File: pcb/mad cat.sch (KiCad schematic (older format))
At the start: 262 parts, among them J1 Conn_01x04, J2 Conn_02x03_Odd_Even, SW0,0 ESC, SW0,1 ESC/F1, SW0,10 F9, SW0,10-1 F10, SW0,11 F10, SW0,11-1 F11, SW0,12 F11, SW0,12-1 F12, SW0,13 F12/PRT, SW0,14 INS, SW0,15 HOME, SW0,16 PGUP, SW0,2 F1, SW0,2-1 F2, SW0,3 F2, SW0,3-1 F3, SW0,4 F3, SW0,4-1 F4, SW0,5 F4, SW0,5-1 F5, SW0,6 F5, SW0,6-1 F6, SW0,7 F6, SW0,7-1 F7, SW0,8 F7, SW0,8-1 F8, SW0,9 F8, SW0,9-1 F9, SW1,0 PF1, SW1,0-1 PF1, SW1,1 TILDE, SW1,10 9, SW1,11 0, SW1,12 -, SW1,13 =, SW1,14 BACKSPACE, SW1,14-1 S_BS_L, SW1,15 END, SW1,16 PGDN, SW1,2 1, SW1,3 2, SW1,4 3, SW1,5 4, SW1,6 5, SW1,7 6, SW1,8 7, SW1,9 8, SW2,0 PF2, SW2,0-1 PF2, SW2,1 TAB, SW2,10 O, SW2,11 P, SW2,12 [, SW2,13 ], SW2,14 \\, SW2,15 S_BS_R, SW2,16 PRT, SW2,2 Q, SW2,3 W, SW2,4 E, SW2,5 R, SW2,6 T, SW2,7 Y, SW2,8 U, SW2,9 I, SW3,0 PF3, SW3,0-1 PF3, SW3,1 CAPS, SW3,1-1 ST_CAPS, SW3,10 L, SW3,11 COLONS, SW3,12 QUOTE, SW3,13 ISO_#, SW3,14 ENT, SW3,14-1 ISO_ENT, SW3,15 DEL, SW3,15-1 DEL, SW3,15-2 DEL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

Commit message: little updates
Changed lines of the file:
@@
 Wire Wire Line
 	400  2750 750  2750
-Connection ~ 750  2750
-Wire Wire Line
-	750  2750 1500 2750
-Connection ~ 1500 2750
 Connection ~ 2250 2750
 Wire Wire Line
@@
 $EndComp
 Connection ~ 1350 3950
-Wire Wire Line
-	1350 3950 1350 3550
 Wire Wire Line
 	750  3950 750  4050
@@
 Wire Wire Line
 	1350 1100 1350 1250
-Wire Wire Line
-	750  1550 750  1250
 Connection ~ 750  1550
 Wire Wire Line
 	950  1250 1350 1250
-Wire Wire Line
-	1350 1250 1350 1550
 Connection ~ 1350 1250
 Wire Wire Line
@@
 Connection ~ 1350 3450
 Wire Wire Line
-	1350 3450 1350 3050
-Wire Wire Line
 	750  3450 750  3550
 Connection ~ 750  3550
@@
 Connection ~ 1350 2950
 Wire Wire Line
-	1350 2950 1350 2550
-Wire Wire Line
 	750  2950 750  3050
 Connection ~ 750  3050
@@
 Connection ~ 1350 2450
 Wire Wire Line
-	1350 2450 1350 2050
-Wire Wire Line
 	750  2450 750  2550
 Connection ~ 750  2550
@@
 Connection ~ 1350 1950
 Wire Wire Line
-	1350 1950 1350 1550
-Wire Wire Line
 	750  1950 750  2050
 Connection ~ 750  2050
@@
 	12000 3450 12000 3550
 Connection ~ 12000 3550
+Wire Wire Line
+	1350 1550 1350 1950
+Wire Wire Line
+	750  1250 750  1550
+Wire Wire Line
+	1350 1250 1350 1550
+Wire Wire Line
+	1350 3550 1350 3950
+Wire Wire Line
+	1350 3050 1350 3450
+Connection ~ 1500 2750
+Connection ~ 750  2750
+Wire Wire Line
+	750  2750 1500 2750
+Wire Wire Line
+	1350 2550 1350 2950
+Wire Wire Line
+	1350 2050 1350 2450
 $EndSCHEMATC

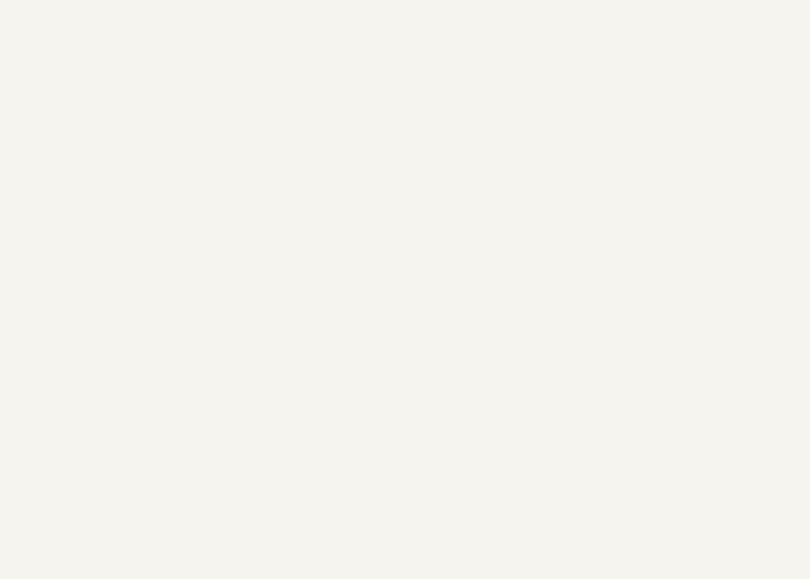
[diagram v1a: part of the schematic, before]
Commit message: changed holes to m2.5
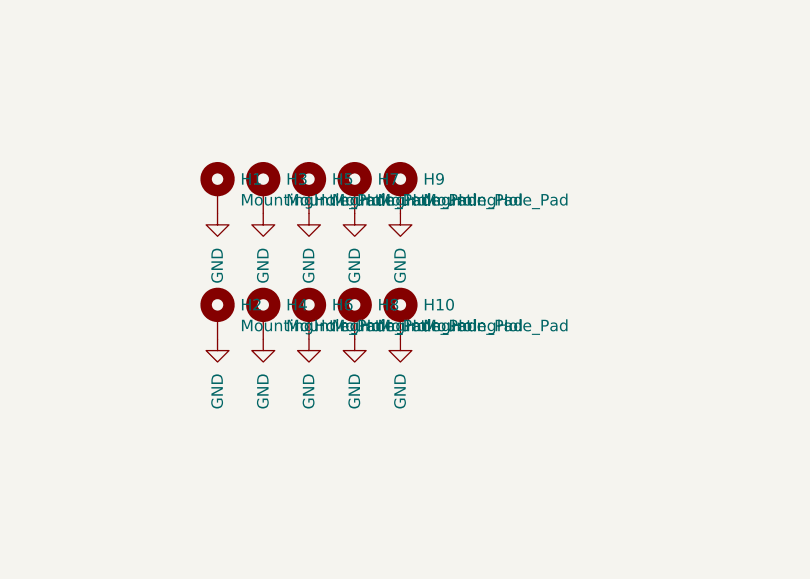
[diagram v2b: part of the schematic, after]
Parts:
- added H1, H10, H2, H3, H4, H5, H6, H7, H8, H9: MountingHole_Pad, keebs:m2.5_pad_via, symbol Mechanical:MountingHole_Pad
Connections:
- net GND: now also H1.1, H10.1, H2.1, H3.1, H4.1, H5.1, H6.1, H7.1, H8.1, H9.1
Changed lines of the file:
@@
 Wire Wire Line
 	1350 2050 1350 2450
+$Comp
+L Mechanical:MountingHole_Pad H1
+U 1 1 5CEC3121
+P 1300 5750
+F 0 "H1" H 1400 5799 50  0000 L CNN
+F 1 "MountingHole_Pad" H 1400 5708 50  0000 L CNN
+F 2 "keebs:m2.5_pad_via" H 1300 5750 50  0001 C CNN
+F 3 "~" H 1300 5750 50  0001 C CNN
+	1    1300 5750
+	1    0    0    -1
+$EndComp
+$Comp
+L power:GND #PWR011
+U 1 1 5CEC4BEC
+P 1300 5850
+F 0 "#PWR011" H 1300 5600 50  0001 C CNN
+F 1 "GND" V 1300 5700 50  0000 R CNN
+F 2 "" H 1300 5850 50  0001 C CNN
+F 3 "" H 1300 5850 50  0001 C CNN
+	1    1300 5850
+	1    0    0    -1
+$EndComp
+$Comp
+L Mechanical:MountingHole_Pad H3
+U 1 1 5CEC7481
+P 1500 5750
+F 0 "H3" H 1600 5799 50  0000 L CNN
+F 1 "MountingHole_Pad" H 1600 5708 50  0000 L CNN
+F 2 "keebs:m2.5_pad_via" H 1500 5750 50  0001 C CNN
+F 3 "~" H 1500 5750 50  0001 C CNN
+	1    1500 5750
+	1    0    0    -1
+$EndComp
+$Comp
+L power:GND #PWR030
+U 1 1 5CEC7487
+P 1500 5850
+F 0 "#PWR030" H 1500 5600 50  0001 C CNN
+F 1 "GND" V 1500 5700 50  0000 R CNN
+F 2 "" H 1500 5850 50  0001 C CNN
+F 3 "" H 1500 5850 50  0001 C CNN
+	1    1500 5850
+	1    0    0    -1
+$EndComp
+$Comp
+L Mechanical:MountingHole_Pad H5
+U 1 1 5CEE69D2
+P 1700 5750
+F 0 "H5" H 1800 5799 50  0000 L CNN
+F 1 "MountingHole_Pad" H 1800 5708 50  0000 L CNN
+F 2 "keebs:m2.5_pad_via" H 1700 5750 50  0001 C CNN
+F 3 "~" H 1700 5750 50  0001 C CNN
+	1    1700 5750
+	1    0    0    -1
+$EndComp
+$Comp
+L power:GND #PWR032
+U 1 1 5CEE69D8
+P 1700 5850
+F 0 "#PWR032" H 1700 5600 50  0001 C CNN
+F 1 "GND" V 1700 5700 50  0000 R CNN
+F 2 "" H 1700 5850 50  0001 C CNN
+F 3 "" H 1700 5850 50  0001 C CNN
+	1    1700 5850
+	1    0    0    -1
+$EndComp
+$Comp
+L Mechanical:MountingHole_Pad H7
+U 1 1 5CF05E57
+P 1900 5750
+F 0 "H7" H 2000 5799 50  0000 L CNN
+F 1 "MountingHole_Pad" H 2000 5708 50  0000 L CNN
+F 2 "keebs:m2.5_pad_via" H 1900 5750 50  0001 C CNN
+F 3 "~" H 1900 5750 50  0001 C CNN
+	1    1900 5750
+	1    0    0    -1
+$EndComp
+$Comp
+L power:GND #PWR034
+U 1 1 5CF05E5D
+P 1900 5850
+F 0 "#PWR034" H 1900 5600 50  0001 C CNN
+F 1 "GND" V 1900 5700 50  0000 R CNN
+F 2 "" H 1900 5850 50  0001 C CNN
+F 3 "" H 1900 5850 50  0001 C CNN
+	1    1900 5850
+	1    0    0    -1
+$EndComp
+$Comp
+L Mechanical:MountingHole_Pad H2
+U 1 1 5CF254C4
+P 1300 6300
+F 0 "H2" H 1400 6349 50  0000 L CNN
+F 1 "MountingHole_Pad" H 1400 6258 50  0000 L CNN
+F 2 "keebs:m2.5_pad_via" H 1300 6300 50  0001 C CNN
+F 3 "~" H 1300 6300 50  0001 C CNN
+	1    1300 6300
+	1    0    0    -1
+$EndComp
+$Comp
+L power:GND #PWR016
+U 1 1 5CF254CA
+P 1300 6400
+F 0 "#PWR016" H 1300 6150 50  0001 C CNN
+F 1 "GND" V 1300 6250 50  0000 R CNN
+F 2 "" H 1300 6400 50  0001 C CNN
+F 3 "" H 1300 6400 50  0001 C CNN
+	1    1300 6400
+	1    0    0    -1
+$EndComp
+$Comp
+L Mechanical:MountingHole_Pad H4
+U 1 1 5CF44A2D
+P 1500 6300
+F 0 "H4" H 1600 6349 50  0000 L CNN
+F 1 "MountingHole_Pad" H 1600 6258 50  0000 L CNN
+F 2 "keebs:m2.5_pad_via" H 1500 6300 50  0001 C CNN
+F 3 "~" H 1500 6300 50  0001 C CNN
+	1    1500 6300
+	1    0    0    -1
+$EndComp
+$Comp
+L power:GND #PWR031
+U 1 1 5CF44A33
+P 1500 6400
+F 0 "#PWR031" H 1500 6150 50  0001 C CNN
+F 1 "GND" V 1500 6250 50  0000 R CNN
+F 2 "" H 1500 6400 50  0001 C CNN
+F 3 "" H 1500 6400 50  0001 C CNN
+	1    1500 6400
+	1    0    0    -1
+$EndComp
+$Comp
+L Mechanical:MountingHole_Pad H6
+U 1 1 5CF64138
+P 1700 6300
+F 0 "H6" H 1800 6349 50  0000 L CNN
+F 1 "MountingHole_Pad" H 1800 6258 50  0000 L CNN
+F 2 "keebs:m2.5_pad_via" H 1700 6300 50  0001 C CNN
+F 3 "~" H 1700 6300 50  0001 C CNN
+	1    1700 6300
+	1    0    0    -1
+$EndComp
+$Comp
+L power:GND #PWR033
+U 1 1 5CF6413E
+P 1700 6400
+F 0 "#PWR033" H 1700 6150 50  0001 C CNN
+F 1 "GND" V 1700 6250 50  0000 R CNN
+F 2 "" H 1700 6400 50  0001 C CNN
+F 3 "" H 1700 6400 50  0001 C CNN
+	1    1700 6400
+	1    0    0    -1
+$EndComp
+$Comp
+L Mechanical:MountingHole_Pad H8
+U 1 1 5CF836A1
+P 1900 6300
+F 0 "H8" H 2000 6349 50  0000 L CNN
+F 1 "MountingHole_Pad" H 2000 6258 50  0000 L CNN
+F 2 "keebs:m2.5_pad_via" H 1900 6300 50  0001 C CNN
+F 3 "~" H 1900 6300 50  0001 C CNN
+	1    1900 6300
+	1    0    0    -1
+$EndComp
+$Comp
+L power:GND #PWR035
+U 1 1 5CF836A7
+P 1900 6400
+F 0 "#PWR035" H 1900 6150 50  0001 C CNN
+F 1 "GND" V 1900 6250 50  0000 R CNN
+F 2 "" H 1900 6400 50  0001 C CNN
+F 3 "" H 1900 6400 50  0001 C CNN
+	1    1900 6400
+	1    0    0    -1
+$EndComp
+$Comp
+L Mechanical:MountingHole_Pad H9
+U 1 1 5CFC6FD9
+P 2100 5750
+F 0 "H9" H 2200 5799 50  0000 L CNN
+F 1 "MountingHole_Pad" H 2200 5708 50  0000 L CNN
+F 2 "keebs:m2.5_pad_via" H 2100 5750 50  0001 C CNN
+F 3 "~" H 2100 5750 50  0001 C CNN
+	1    2100 5750
+	1    0    0    -1
+$EndComp
+$Comp
+L power:GND #PWR036
+U 1 1 5CFC6FDF
+P 2100 5850
+F 0 "#PWR036" H 2100 5600 50  0001 C CNN
+F 1 "GND" V 2100 5700 50  0000 R CNN
+F 2 "" H 2100 5850 50  0001 C CNN
+F 3 "" H 2100 5850 50  0001 C CNN
+	1    2100 5850
+	1    0    0    -1
+$EndComp
+$Comp
+L Mechanical:MountingHole_Pad H10
+U 1 1 5CFE6828
+P 2100 6300
+F 0 "H10" H 2200 6349 50  0000 L CNN
+F 1 "MountingHole_Pad" H 2200 6258 50  0000 L CNN
+F 2 "keebs:m2.5_pad_via" H 2100 6300 50  0001 C CNN
+F 3 "~" H 2100 6300 50  0001 C CNN
+	1    2100 6300
+	1    0    0    -1
+$EndComp
+$Comp
+L power:GND #PWR037
+U 1 1 5CFE682E
+P 2100 6400
+F 0 "#PWR037" H 2100 6150 50  0001 C CNN
+F 1 "GND" V 2100 6250 50  0000 R CNN
+F 2 "" H 2100 6400 50  0001 C CNN
+F 3 "" H 2100 6400 50  0001 C CNN
+	1    2100 6400
+	1    0    0    -1
+$EndComp
 $EndSCHEMATC

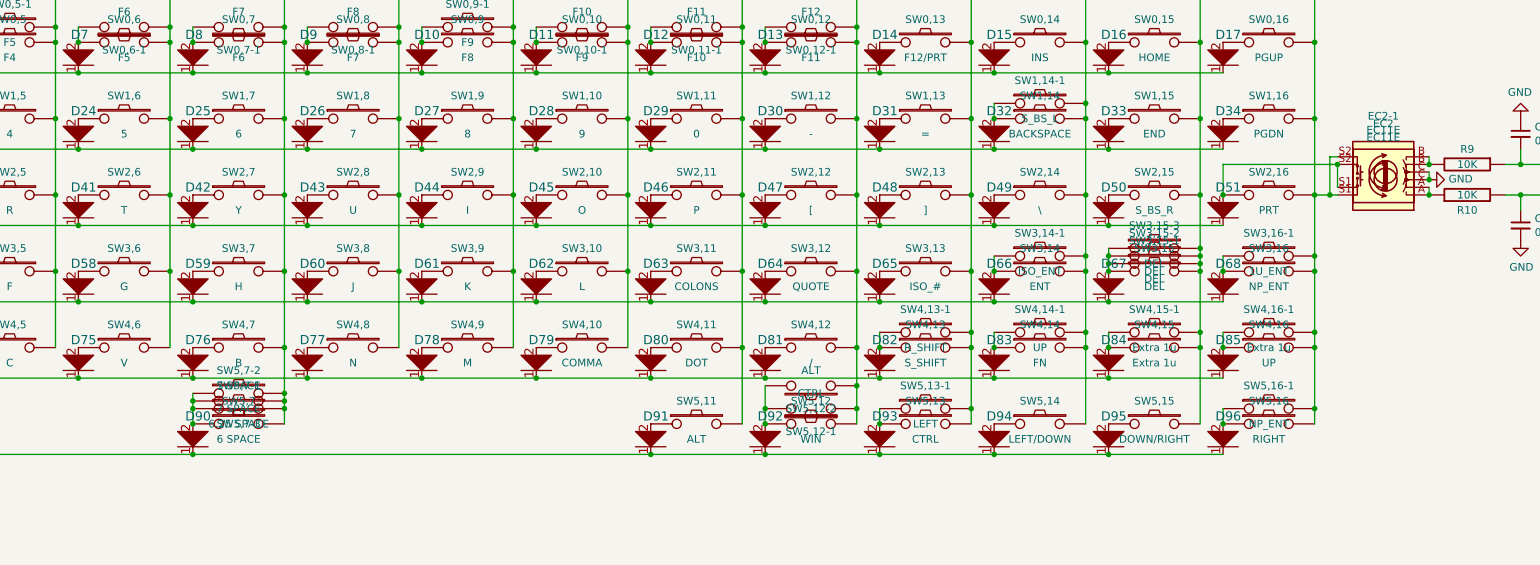
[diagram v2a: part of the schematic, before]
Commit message: redo layout after ic
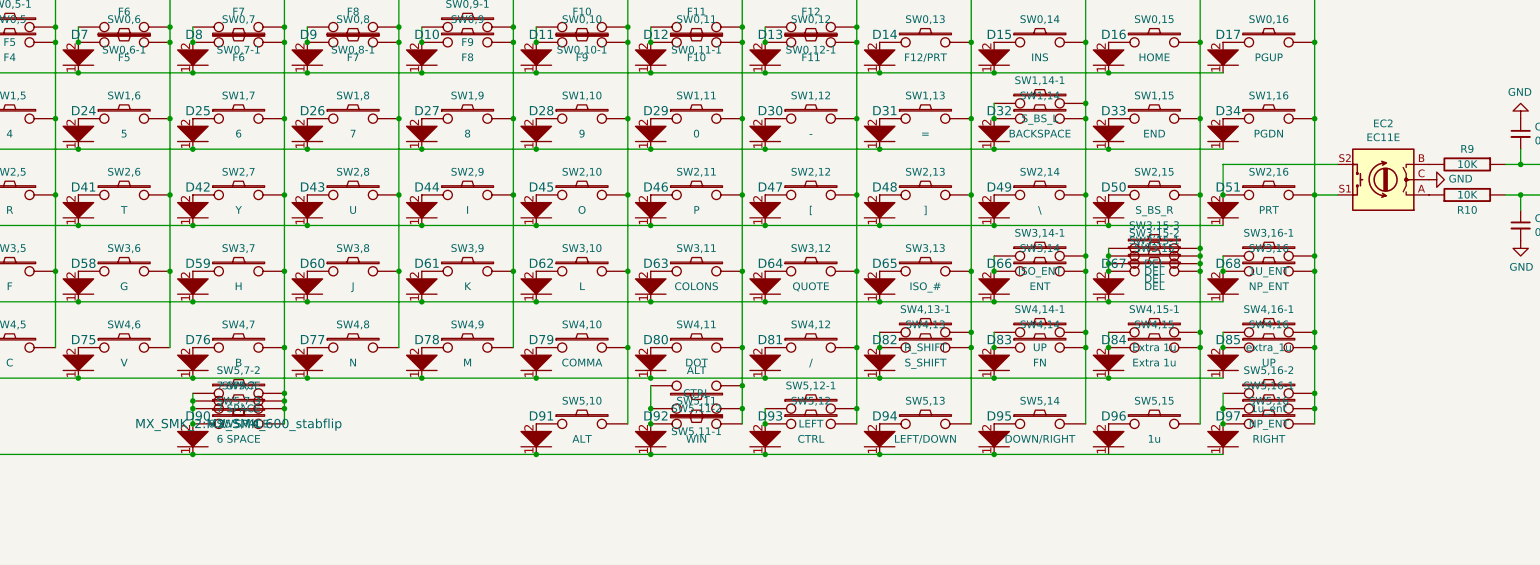
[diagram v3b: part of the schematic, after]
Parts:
- removed EC2-1: EC11E, keebs:EC11E, symbol Device:Rotary_Encoder_Switch
- removed SW5,7: 6 SPACE, MX_SMK_2:MX_600_stabflip, symbol keyboard_parts:SW_PUSH
- added D96: D, Diode_SMD:D_SOD-123, symbol keyboard_parts:D
- added SW5,15: 1u, MX_SMK_2:MX_100, symbol keyboard_parts:SW_PUSH
- added SW5,16-2: 1u_ent, MX_SMK_2:MX_100, symbol keyboard_parts:SW_PUSH
- added SW5,7-3: 6 SPACE, MX_SMK_2:MX_SMK_600_stabflip, symbol keyboard_parts:SW_PUSH
- SW3,15, SW3,15-1: footprint MX_SMK_2:MX_200 -> MX_SMK_2:MX_200_stabflip
- SW4,16-1: value Extra 1u -> extra_1u
- renumbered D96 to D97, SW5,11 to SW5,10, SW5,12 to SW5,11, SW5,12-1 to SW5,11-1, SW5,12-2 to SW5,11-2, SW5,13 to SW5,12, SW5,13-1 to SW5,12-1, SW5,14 to SW5,13, SW5,15 to SW5,14, SW5,7-1 to SW5,7, SW5,7-3 to SW5,7-1
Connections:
- net c10: now also SW5,10.2
- net c11: now also SW5,11-1.1, SW5,11-2.1, SW5,11.2; no longer SW5,10.2
- net c12: now also SW5,12-1.2, SW5,12.2; no longer SW5,11-1.1, SW5,11-2.1, SW5,11.2
- net c13: now also SW5,13.2; no longer SW5,12-1.2, SW5,12.2
- net c14: now also SW5,14.2; no longer SW5,13.2
- net c15: now also SW5,15.2; no longer SW5,14.2
- net c16: now also SW5,16-2.2
- net c7: now also SW5,7-3.2
- net at D90.2, SW5,7-1.2, SW5,7-2.1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: now also SW5,7-3.1
- net at D97.2, SW5,16-1.1, SW5,16.1: now also SW5,16-2.1
- new net: D96.2, SW5,15.1
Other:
- moved on the sheet: D91, D92, D93, D94, D95, SW5,10, SW5,11, SW5,11-1, SW5,11-2, SW5,12, SW5,12-1, SW5,13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

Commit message: progress on redo
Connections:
- net r5: now also D96.1
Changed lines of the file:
@@
 Connection ~ 11250 4250
 Wire Wire Line
-	11250 4250 12750 4250
+	11250 4250 12000 4250
 $Comp
 L keyboard_parts:SW_PUSH SW5,15
@@
 $EndComp
 Connection ~ 6000 4050
+Connection ~ 12000 4250
+Wire Wire Line
+	12000 4250 12750 4250
 $EndSCHEMATC

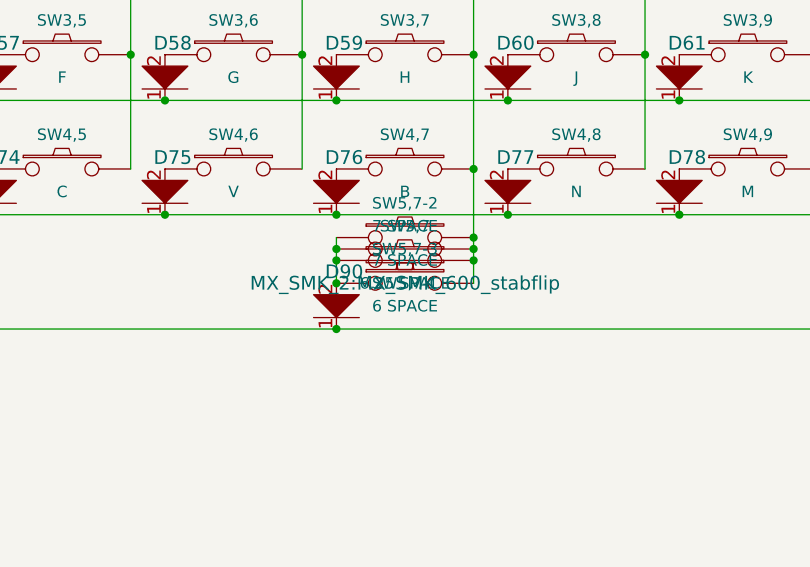
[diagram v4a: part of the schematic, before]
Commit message: via stitched proto
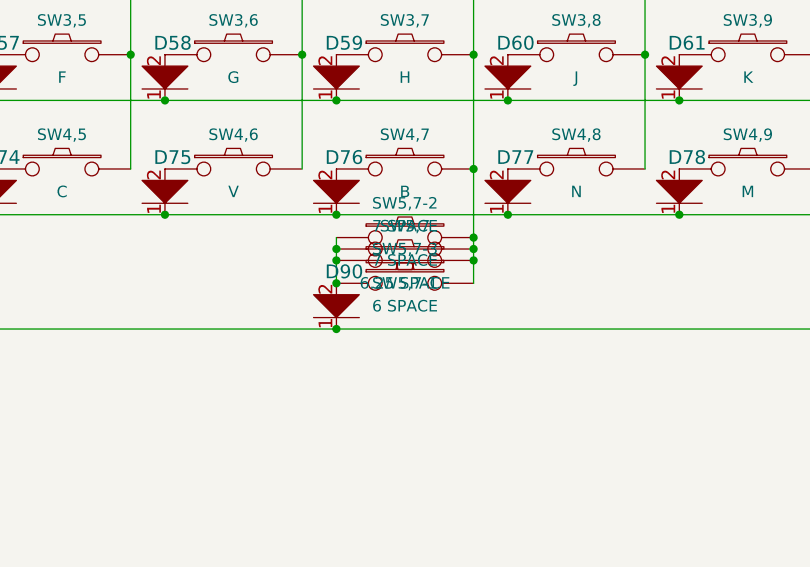
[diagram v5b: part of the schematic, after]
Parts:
- SW5,7-3: footprint MX_SMK_2:MX_SMK_600_stabflip -> MX_SMK_2:MX_100
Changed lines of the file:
@@
 	10500 4250 11250 4250
 Connection ~ 11250 4250
-Wire Wire Line
-	11250 4250 12000 4250
 $Comp
 L keyboard_parts:SW_PUSH SW5,15
@@
 F 0 "SW5,7-3" H 6300 4200 50  0000 C CNN
 F 1 "6 SPACE" H 6300 3950 50  0000 C CNN
-F 2 "MX_SMK_2:MX_SMK_600_stabflip" H 6300 4050 60  0000 C CNN
+F 2 "MX_SMK_2:MX_100" H 6300 3950 60  0001 C CNN
 F 3 "" H 6300 4050 60  0000 C CNN
 	1    6300 4050
@@
 $EndComp
 Connection ~ 6000 4050
+Wire Wire Line
+	11250 4250 12000 4250
 Connection ~ 12000 4250
 Wire Wire Line

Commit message: design done for proto
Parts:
- removed SW5,11-2, SW5,2-2: ALT, MX_SMK_2:MX_150, symbol keyboard_parts:SW_PUSH
- removed SW5,7-1: 7 SPACE, MX_SMK_2:MX_700_stabflip, symbol keyboard_parts:SW_PUSH
- EC1, EC2: footprint keebs:EC11E -> keebs:EC11E_offset
- SW5,7-2: footprint MX_SMK_2:MX_700_stabflip -> MX_SMK_2:MX_100
- SW5,7-3: footprint MX_SMK_2:MX_100 -> MX_SMK_2:MX_600_stabflip
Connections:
- net c11: now also SW5,11-1.2; no longer SW5,11-1.1
- net c7: now also SW5,7-2.1; no longer SW5,7-2.2
- net at D90.2, SW5,7-3.1, SW5,7.1: now also SW5,7-2.2; no longer SW5,7-2.1
- net at D92.2, SW5,11.1: now also SW5,11-1.1; no longer SW5,11-1.2
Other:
- moved on the sheet: SW5,11-1, SW5,7-2
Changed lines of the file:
@@
 F 0 "EC2" H 13800 2083 50  0000 C CNN
 F 1 "EC11E" H 13800 2174 50  0000 C CNN
-F 2 "keebs:EC11E" H 13650 2610 50  0001 C CNN
+F 2 "keebs:EC11E_offset" H 13650 2610 50  0001 C CNN
 F 3 "~" H 13800 2710 50  0001 C CNN
 	1    13800 2450
@@
 F 0 "EC1" V 804 1180 50  0000 L CNN
 F 1 "EC11E" V 895 1180 50  0000 L CNN
-F 2 "keebs:EC11E" H 700 1110 50  0001 C CNN
+F 2 "keebs:EC11E_offset" H 700 1110 50  0001 C CNN
 F 3 "~" H 850 1210 50  0001 C CNN
 	1    850  950
@@
 	-1   0    0    1
 $EndComp
-Wire Wire Line
-	6600 4050 6600 3950
 Connection ~ 6600 1550
 Connection ~ 6600 2050
@@
 	-1   0    0    1
 $EndComp
-Wire Wire Line
-	9600 4050 9600 3950
 Connection ~ 9600 1550
 Wire Wire Line
@@
 	1    0    0    -1
 $EndComp
-Connection ~ 6600 3950
-Wire Wire Line
-	6600 3950 6600 3900
 Wire Wire Line
 	6000 3950 6000 4050
@@
 F 3 "" H 9300 3950 60  0000 C CNN
 	1    9300 3950
-	-1   0    0    1
+	1    0    0    -1
 $EndComp
 $Comp
@@
 Connection ~ 2850 3950
 Wire Wire Line
-	2850 3950 2850 3850
-Wire Wire Line
 	2250 3950 2250 4050
 Connection ~ 2250 4050
@@
 Connection ~ 12000 3050
 $Comp
-L keyboard_parts:SW_PUSH SW5,11-2
-U 1 1 5CE261EE
-P 9300 3800
-F 0 "SW5,11-2" H 9300 3950 50  0000 C CNN
-F 1 "ALT" H 9300 3700 50  0000 C CNN
-F 2 "MX_SMK_2:MX_150" H 9300 3800 60  0001 C CNN
-F 3 "" H 9300 3800 60  0000 C CNN
-	1    9300 3800
-	-1   0    0    1
-$EndComp
-$Comp
 L keyboard_parts:SW_PUSH SW5,7-2
 U 1 1 5CE4437C
@@
 F 0 "SW5,7-2" H 6300 4000 50  0000 C CNN
 F 1 "7 SPACE" H 6300 3750 50  0000 C CNN
-F 2 "MX_SMK_2:MX_700_stabflip" H 6300 3850 60  0001 C CNN
+F 2 "MX_SMK_2:MX_100" H 6300 3850 60  0001 C CNN
 F 3 "" H 6300 3850 60  0000 C CNN
 	1    6300 3850
-	1    0    0    -1
-$EndComp
-Connection ~ 6600 3850
-Wire Wire Line
-	6600 3850 6600 3550
-Wire Wire Line
-	6000 3850 6000 3900
-Connection ~ 6000 3950
-$Comp
-L keyboard_parts:SW_PUSH SW5,2-2
-U 1 1 5CDD1EA0
-P 2550 3850
-F 0 "SW5,2-2" H 2550 4000 50  0000 C CNN
-F 1 "ALT" H 2550 3750 50  0000 C CNN
-F 2 "MX_SMK_2:MX_150" H 2550 3850 60  0001 C CNN
-F 3 "" H 2550 3850 60  0000 C CNN
-	1    2550 3850
-	-1   0    0    1
-$EndComp
-Connection ~ 2850 3850
-Wire Wire Line
-	2850 3850 2850 3550
-Wire Wire Line
-	2250 3850 2250 3950
-Connection ~ 2250 3950
-$Comp
-L keyboard_parts:SW_PUSH SW5,7-1
-U 1 1 5CDF148D
-P 6300 3900
-F 0 "SW5,7-1" H 6300 4050 50  0000 C CNN
-F 1 "7 SPACE" H 6300 3800 50  0000 C CNN
-F 2 "MX_SMK_2:MX_700_stabflip" H 6300 3900 60  0001 C CNN
-F 3 "" H 6300 3900 60  0000 C CNN
-	1    6300 3900
 	-1   0    0    1
 $EndComp
-Connection ~ 6600 3900
-Wire Wire Line
-	6600 3900 6600 3850
-Connection ~ 6000 3900
-Wire Wire Line
-	6000 3900 6000 3950
+Connection ~ 6000 3950
 $Comp
 L mad-cat-rescue:TC33X-2-103E-dk_Trimmer-Potentiometers POT1
@@
 Connection ~ 8850 3550
 Connection ~ 9000 4250
-Connection ~ 9600 3800
-Wire Wire Line
-	9600 3800 9600 3550
-Connection ~ 9600 3950
-Wire Wire Line
-	9600 3950 9600 3800
-Wire Wire Line
-	9000 4250 9750 4250
-Wire Wire Line
-	9000 3800 9000 3950
 Wire Wire Line
 	10350 3550 10350 3950
-Connection ~ 9000 3950
 Wire Wire Line
 	9000 3950 9000 4050
@@
 	1    0    0    -1
 $EndComp
+Wire Wire Line
+	11250 4250 12000 4250
+Connection ~ 12000 4250
+Wire Wire Line
+	12000 4250 12750 4250
 $Comp
 L keyboard_parts:SW_PUSH SW5,7-3
-U 1 1 5D89B8C2
+U 1 1 5D08BA56
 P 6300 4050
 F 0 "SW5,7-3" H 6300 4200 50  0000 C CNN
 F 1 "6 SPACE" H 6300 3950 50  0000 C CNN
-F 2 "MX_SMK_2:MX_100" H 6300 3950 60  0001 C CNN
+F 2 "MX_SMK_2:MX_600_stabflip" H 6300 4050 60  0001 C CNN
 F 3 "" H 6300 4050 60  0000 C CNN
 	1    6300 4050
@@
 Connection ~ 6000 4050
 Wire Wire Line
-	11250 4250 12000 4250
-Connection ~ 12000 4250
+	6600 3950 6600 4050
+Connection ~ 6600 3950
 Wire Wire Line
-	12000 4250 12750 4250
+	2850 3550 2850 3950
+Wire Wire Line
+	6000 3850 6000 3950
+Wire Wire Line
+	6600 3550 6600 3850
+Connection ~ 6600 3850
+Wire Wire Line
+	6600 3850 6600 3950
+Wire Wire Line
+	9600 3550 9600 3950
+Connection ~ 9600 3950
+Wire Wire Line
+	9600 3950 9600 4050
+Wire Wire Line
+	9000 4250 9750 4250
 $EndSCHEMATC
